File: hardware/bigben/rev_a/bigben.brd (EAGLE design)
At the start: 25.6 x 13 mm, 13 parts, among them J3 IMPULSE_GECKO_HEADER, U1 RV-3049-C3, U2 FM25LBTDFN-8

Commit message: bigben documentation
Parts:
- moved R1 0.38 mm to (18.9, 1.83)
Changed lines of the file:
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@@
 <element name="U2" library="chips" package="TDFN-8" value="FM25LBTDFN-8" x="23.5962" y="3.6322" smashed="yes">
 <attribute name="MOUSER" value="877-FM25V20-DG" x="23.5962" y="3.6322" size="1.778" layer="27" display="off"/>
-<attribute name="NAME" x="25.0522" y="1.201" size="0.762" layer="25" font="vector" ratio="12" rot="R180" align="bottom-center"/>
+<attribute name="NAME" x="22.0042" y="1.201" size="0.762" layer="25" font="vector" ratio="12" rot="R180" align="bottom-center"/>
 <attribute name="VALUE" x="23.5962" y="0.2322" size="0.508" layer="27" font="vector" ratio="12" align="bottom-center"/>
 </element>
-<element name="R1" library="passives" package="0402_RES" value="4.7k" x="19.3294" y="1.8288" smashed="yes" rot="R90">
-<attribute name="NAME" x="19.3294" y="1.0922" size="0.762" layer="25" font="vector" ratio="12" rot="R90" align="center-right"/>
-<attribute name="VALUE" x="19.7104" y="0.3048" size="0.508" layer="27" font="vector" ratio="12" rot="R90" align="bottom-center"/>
+<element name="R1" library="passives" package="0402_RES" value="4.7k" x="18.9484" y="1.8288" smashed="yes" rot="R90">
+<attribute name="NAME" x="18.669" y="1.8288" size="0.762" layer="25" font="vector" ratio="12" rot="R90" align="bottom-center"/>
+<attribute name="VALUE" x="19.3294" y="0.3048" size="0.508" layer="27" font="vector" ratio="12" rot="R90" align="bottom-center"/>
 </element>
 <element name="R2" library="passives" package="0402_RES" value="4.7k" x="22.9112" y="6.6728" smashed="yes" rot="R180">
@@
 </element>
 <element name="R3" library="passives" package="0402_RES" value="4.7k" x="20.3454" y="1.8288" smashed="yes" rot="R90">
-<attribute name="NAME" x="20.3348" y="1.093" size="0.762" layer="25" font="vector" ratio="12" rot="R270" align="center-left"/>
+<attribute name="NAME" x="20.03" y="1.8296" size="0.762" layer="25" font="vector" ratio="12" rot="R270" align="top-center"/>
 <attribute name="VALUE" x="21.7424" y="1.8288" size="0.508" layer="27" font="vector" ratio="12" rot="R90" align="bottom-center"/>
 </element>
@@
 </element>
 <element name="R6" library="passives" package="0402_RES" value="10k" x="26.8732" y="12.1666" smashed="yes" rot="R180">
-<attribute name="NAME" x="26.8732" y="12.5222" size="0.762" layer="25" font="vector" ratio="12" align="bottom-center"/>
+<attribute name="NAME" x="26.8732" y="11.8618" size="0.762" layer="25" font="vector" ratio="12" rot="R180" align="bottom-center"/>
 <attribute name="VALUE" x="26.8732" y="13.5636" size="1.016" layer="27" font="vector" ratio="12" rot="R180" align="bottom-center"/>
 </element>
@@
 </element>
 <element name="R4" library="passives" package="0402_RES" value="4.7k" x="29.337" y="12.1666" smashed="yes">
-<attribute name="NAME" x="29.337" y="12.5476" size="0.762" layer="25" font="vector" ratio="12" align="bottom-center"/>
+<attribute name="NAME" x="29.6926" y="11.8618" size="0.762" layer="25" font="vector" ratio="12" rot="R180" align="bottom-center"/>
 <attribute name="VALUE" x="29.337" y="10.7696" size="1.016" layer="27" font="vector" ratio="12" align="bottom-center"/>
 </element>
@@
 <via x="25.8572" y="4.1656" extent="1-16" drill="0.2032"/>
 <via x="25.8572" y="3.0734" extent="1-16" drill="0.2032"/>
-<via x="19.7358" y="4.2672" extent="1-16" drill="0.2032"/>
+<via x="19.5326" y="3.937" extent="1-16" drill="0.2032"/>
 <via x="20.2946" y="7.0104" extent="1-16" drill="0.4064"/>
 <via x="23.7744" y="10.9982" extent="1-16" drill="0.4064"/>
@@
 <wire x1="21.336" y1="4.6482" x2="19.8374" y2="3.1496" width="0.4064" layer="16"/>
 <wire x1="19.8374" y1="2.76986875" x2="20.3454" y2="2.26186875" width="0.4064" layer="1"/>
-<wire x1="19.3294" y1="2.26186875" x2="19.8374" y2="2.76986875" width="0.4064" layer="1"/>
 <wire x1="19.8374" y1="2.76986875" x2="19.8374" y2="3.1496" width="0.4064" layer="1"/>
 <wire x1="31.369" y1="6.477" x2="30.9626" y2="6.477" width="0.4064" layer="1"/>
@@
 <wire x1="29.5148" y1="7.9248" x2="28.7782" y2="7.9248" width="0.4064" layer="1"/>
 <wire x1="28.7782" y1="7.9248" x2="23.0378" y2="7.9248" width="0.4064" layer="16"/>
+<wire x1="19.8374" y1="2.76986875" x2="19.3294" y2="2.26186875" width="0.4064" layer="1"/>
+<wire x1="19.3294" y1="2.26186875" x2="18.9484" y2="2.26186875" width="0.4064" layer="1"/>
 </signal>
 <signal name="N$2">
@@
 <contactref element="J3" pad="2"/>
 <via x="29.0322" y="9.906" extent="1-16" drill="0.2032"/>
-<wire x1="23.749" y1="9.4996" x2="18.542" y2="4.2926" width="0.1524" layer="16"/>
-<wire x1="19.3294" y1="1.39573125" x2="19.3294" y2="1.2192" width="0.1524" layer="1"/>
+<wire x1="18.9484" y1="1.39573125" x2="19.3294" y2="1.2192" width="0.1524" layer="1"/>
 <wire x1="19.3294" y1="1.2192" x2="19.9644" y2="0.5842" width="0.1524" layer="1"/>
 <wire x1="19.9644" y1="0.5842" x2="21.0732" y2="0.5842" width="0.1524" layer="1"/>
 <wire x1="21.0732" y1="0.5842" x2="22.1712" y2="1.6822" width="0.1524" layer="1"/>
-<wire x1="18.542" y1="4.2926" x2="18.542" y2="1.27" width="0.1524" layer="16"/>
-<via x="18.542" y="1.27" extent="1-16" drill="0.2032"/>
-<wire x1="18.542" y1="1.27" x2="18.66773125" y2="1.39573125" width="0.1524" layer="1"/>
-<wire x1="18.66773125" y1="1.39573125" x2="19.3294" y2="1.39573125" width="0.1524" layer="1"/>
+<via x="18.9738" y="3.1496" extent="1-16" drill="0.2032"/>
+<wire x1="18.66773125" y1="1.39573125" x2="18.9484" y2="1.39573125" width="0.1524" layer="1"/>
 <wire x1="27.7114" y1="10.1854" x2="27.0256" y2="9.4996" width="0.1524" layer="16"/>
 <wire x1="27.0256" y1="9.4996" x2="23.749" y2="9.4996" width="0.1524" layer="16"/>
@@
 <wire x1="27.7114" y1="10.1854" x2="28.7528" y2="10.1854" width="0.1524" layer="16"/>
 <wire x1="28.7528" y1="10.1854" x2="29.0322" y2="9.906" width="0.1524" layer="16"/>
+<wire x1="18.66773125" y1="1.39573125" x2="18.3642" y2="1.6992625" width="0.1524" layer="1"/>
+<wire x1="18.3642" y1="1.6992625" x2="18.3642" y2="2.8702" width="0.1524" layer="1"/>
+<wire x1="18.3642" y1="2.8702" x2="18.6436" y2="3.1496" width="0.1524" layer="1"/>
+<wire x1="18.6436" y1="3.1496" x2="18.9738" y2="3.1496" width="0.1524" layer="1"/>
+<wire x1="23.749" y1="9.4996" x2="18.9738" y2="4.7244" width="0.1524" layer="16"/>
+<wire x1="18.9738" y1="4.7244" x2="18.9738" y2="3.1496" width="0.1524" layer="16"/>
 </signal>
 <signal name="!FRAM_HOLD">

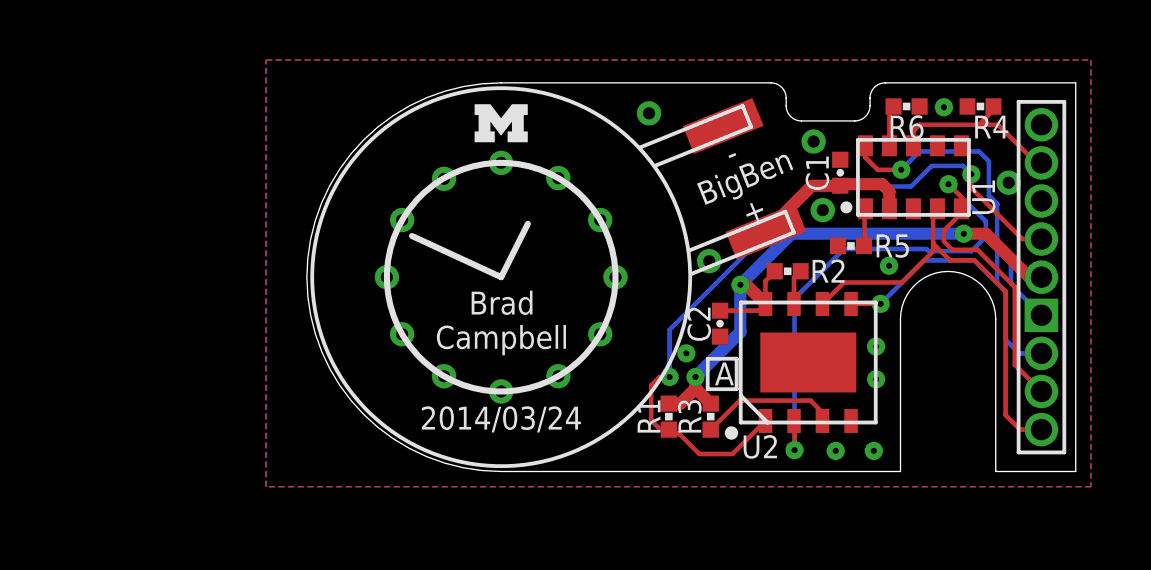
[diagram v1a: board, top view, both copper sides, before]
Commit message: added milling layer for panel to bigben
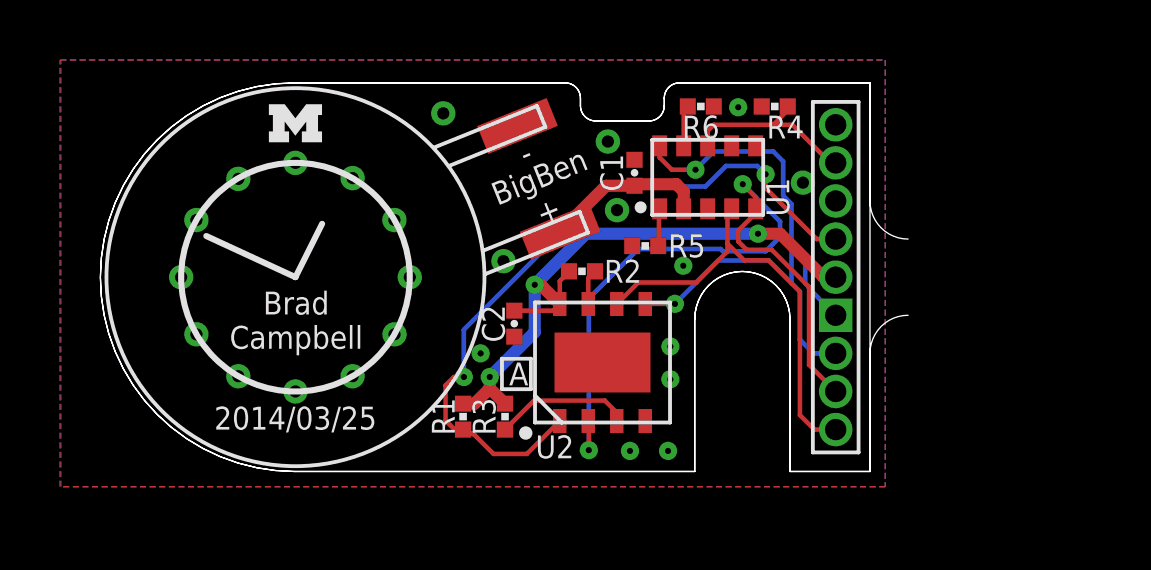
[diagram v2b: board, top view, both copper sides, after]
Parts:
- moved R3 6.86 mm to (13.5, 1.83)
- moved BT1 6.86 mm to (6.50, 6.48)
- moved C1 6.86 mm to (17.8, 9.96)
- moved C2 6.86 mm to (13.8, 4.93)
- moved J3 6.86 mm to (24.5, 6.48)
- moved LOGO1 6.86 mm to (6.50, 11.6)
- moved R2 6.86 mm to (16.1, 6.67)
- moved R4 6.86 mm to (22.5, 12.2)
- moved R6 6.86 mm to (20.0, 12.2)
- moved U1 6.86 mm to (20.2, 9.80)
- moved U2 6.86 mm to (16.7, 3.63)
- moved R1 6.86 mm to (12.1, 1.83)
- moved R5 6.86 mm to (18.2, 7.52)
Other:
- board size 25.6 x 13 mm -> 26.9 x 13 mm
- board text added: "2014/03/25"
- board text removed: "2014/03/24"

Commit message: shipped bigben
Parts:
- removed R5, R6: 10k, passives:0402_RES
- R3, R4: value 4.7k -> 10k
- U2: value FM25LBTDFN-8 -> FM25V20-DG; device chips:TDFN-8 -> chips:TDFN-8/6MM
- moved R2 8.65 mm to (22.7, 12.2), turned to 0 degrees
- moved R3 7.67 mm to (18.2, 7.85), turned to 0 degrees
- moved R4 2.21 mm to (20.3, 12.2), turned to 180 degrees
- moved R1 1.91 mm to (14.0, 2.18)
- moved U2 0.38 mm to (17.1, 3.76)
- moved C1 0.25 mm to (18.1, 9.96)
- moved J3 0.25 mm to (24.8, 6.48)
- moved U1 0.25 mm to (20.5, 9.80)
- moved C2 0.18 mm to (14.0, 5.00), turned to 90 degrees
- turned BT1 to 23.5 degrees
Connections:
- removed net !FRAM_HOLD: R2.1, U2.7
- removed net !FRAM_WP: R3.1, U2.3
- net GND: now also R2.1, R3.1; no longer R5.1, R6.1
- net N$6: now also R4.2; no longer R6.2
- net N$7: now also R3.2; no longer R5.2
- net RTC_CS: now also R2.2; no longer R4.2
- net VCC: now also U2.3, U2.7; no longer R2.2, R3.2
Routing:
- net VCC: track 21.2 -> 26.3 mm
- net !FRAM_WP: track 4.57 -> 0.00 mm
- net !FRAM_CS: track 24.1 -> 20.9 mm
- net !FRAM_HOLD: track 1.18 -> 0.00 mm
- net MOSI0: track 18.4 -> 17.4 mm
- net MISO0: track 24.8 -> 23.9 mm
- net SCLK0: track 14.5 -> 15.0 mm
- net GND: vias 24 -> 20
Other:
- board size 26.9 x 13 mm -> 27.2 x 14.2 mm
